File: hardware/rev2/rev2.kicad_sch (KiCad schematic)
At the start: 31 parts, among them J2 SMA, J3 SMA, J4 Antenna RF and GNSS Data, J5 Antenna GND, J7 USB_C_Receptacle_USB2.0_16P, U4 EClamp2522P

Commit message: continued routing and layouting
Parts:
- removed R24, R25: 0R, Resistor_SMD:R_0603_1608Metric_Pad0.98x0.95mm_HandSolder, symbol Device:R
- renumbered J7 to J1, R10 to R1, R11 to R2, R22 to R3, R23 to R4, U4 to U1
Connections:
- net USB_D+: now also U1.5 (DM_Out)
- net USB_D-: now also U1.4 (DP_Out)
- net D-: now reaches J1.A7 (D-), J1.B7 (D-), R3.1
- net D-*: now reaches R3.2, U1.3 (DP_In)
- net D+*: now reaches R4.2, U1.2 (DM_In)
- net D+: now reaches J1.A6 (D+), J1.B6 (D+), R4.1

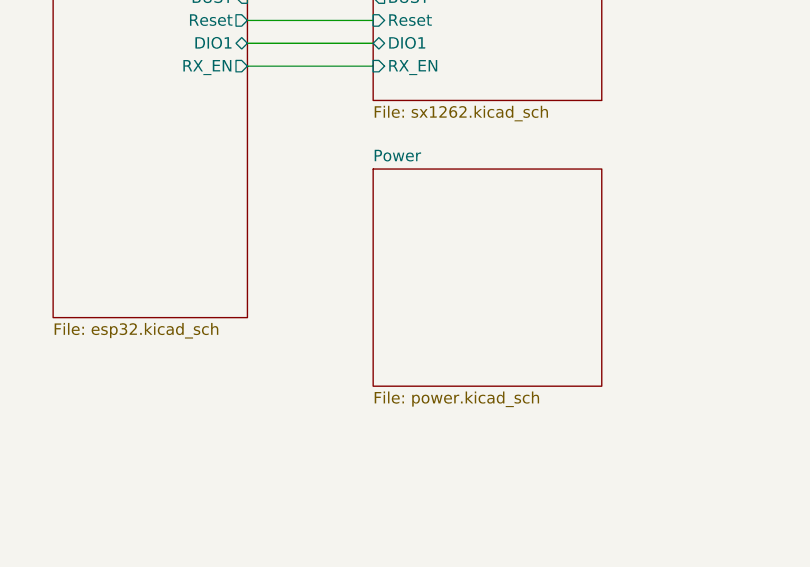
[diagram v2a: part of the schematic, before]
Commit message: Small modifications to power schematic
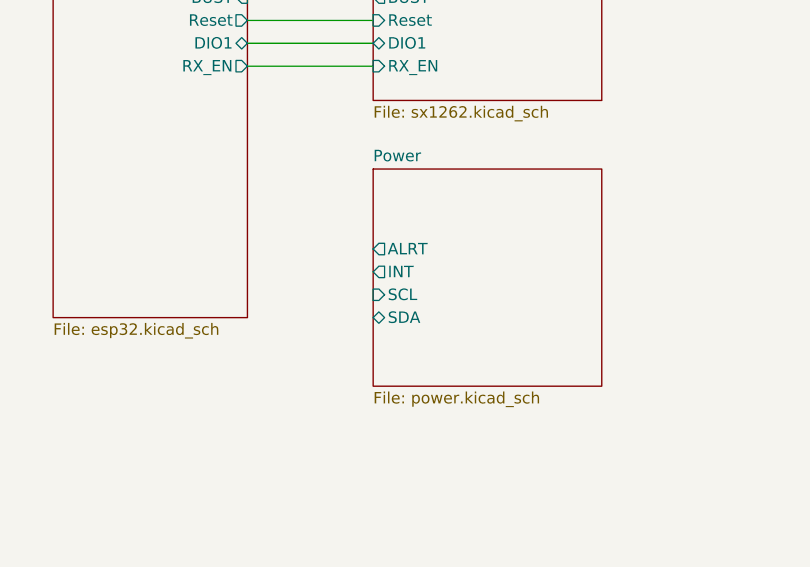
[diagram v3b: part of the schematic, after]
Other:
- sheet Power ports: added ALRT, INT, SCL, SDA; removed none
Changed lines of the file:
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@@
+			)
+		)
+		(pin "ALRT" output
+			(at 173.99 116.84 180)
+			(effects
+				(font
+					(size 1.27 1.27)
+				)
+				(justify left)
+			)
+		)
+		(pin "INT" output
+			(at 173.99 119.38 180)
+			(effects
+				(font
+					(size 1.27 1.27)
+				)
+				(justify left)
+			)
+		)
+		(pin "SCL" input
+			(at 173.99 121.92 180)
+			(effects
+				(font
+					(size 1.27 1.27)
+				)
+				(justify left)
+			)
+		)
+		(pin "SDA" bidirectional
+			(at 173.99 124.46 180)
+			(effects
+				(font
+					(size 1.27 1.27)
+				)
+				(justify left)
 			)
 		)

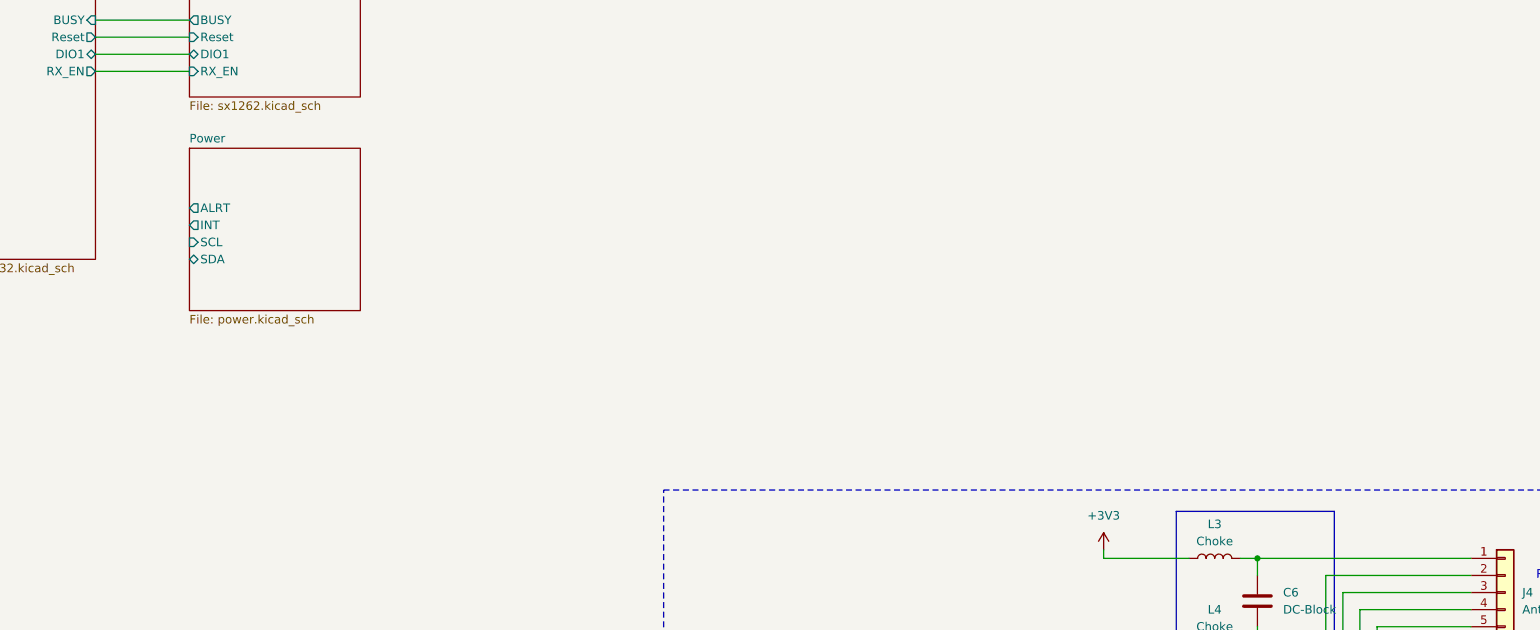
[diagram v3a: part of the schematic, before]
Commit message: continued layout, finished most of the RF stuff
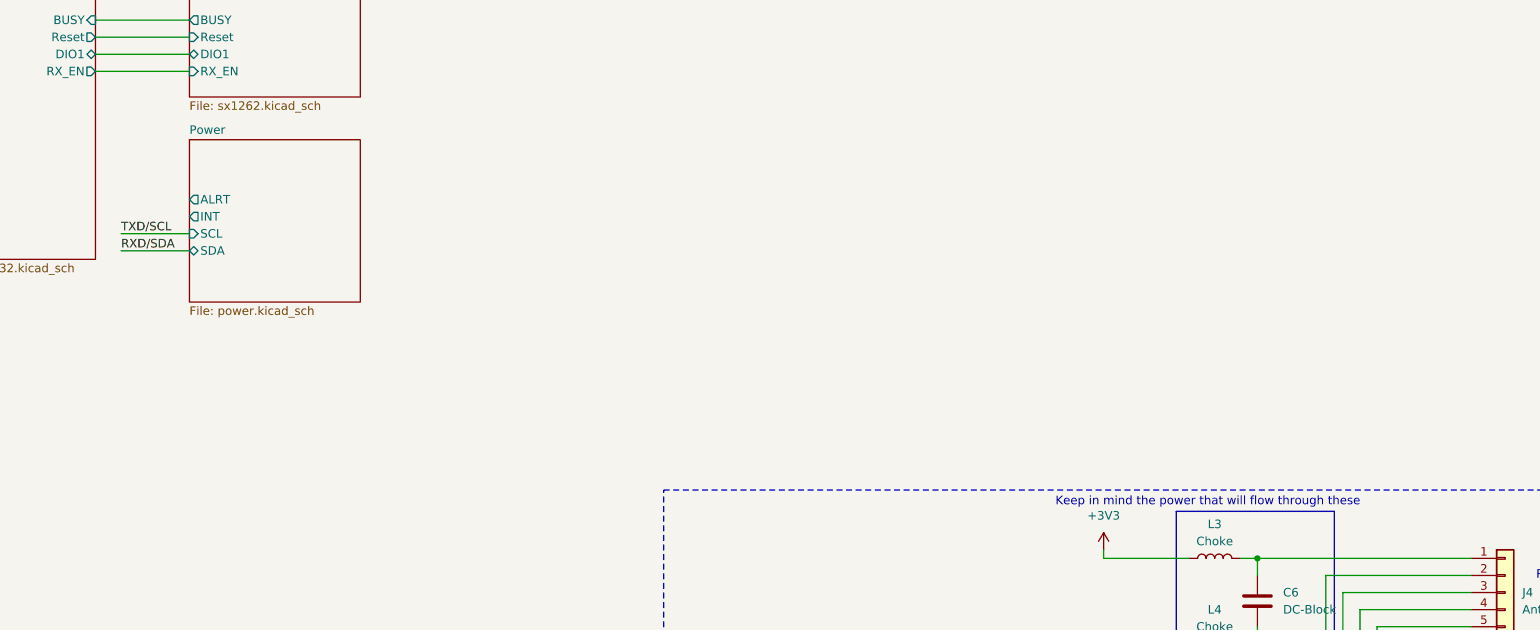
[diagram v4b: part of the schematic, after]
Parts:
- J4, J5: footprint (none) -> _footprints:Antenna_Conn
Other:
- note added: "Keep in mind the power that will flow through these"
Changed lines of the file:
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@@
 		)
 	)
+	(text "Keep in mind the power that will flow through these"
+		(exclude_from_sim no)
+		(at 325.374 160.528 0)
+		(effects
+			(font
+				(size 1.27 1.27)
+			)
+		)
+	)
 	(text "Antenna matching"
 		(exclude_from_sim no)
@@
 	(wire
 		(pts
+			(xy 163.83 123.19) (xy 173.99 123.19)
+		)
+		(stroke
+			(width 0)
+			(type default)
+		)
+	)
+	(wire
+		(pts
 			(xy 309.88 207.01) (xy 322.58 207.01)
 		)
@@
 	(wire
 		(pts
+			(xy 163.83 120.65) (xy 173.99 120.65)
+		)
+		(stroke
+			(width 0)
+			(type default)
+		)
+	)
+	(wire
+		(pts
 			(xy 364.49 195.58) (xy 364.49 198.12)
 		)
@@
 		)
 	)
+	(label "RXD{slash}SDA"
+		(at 163.83 123.19 0)
+		(effects
+			(font
+				(size 1.27 1.27)
+			)
+			(justify left bottom)
+		)
+	)
 	(label "TXD{slash}SCL"
 		(at 173.99 63.5 180)
@@
 		)
 	)
+	(label "TXD{slash}SCL"
+		(at 163.83 120.65 0)
+		(effects
+			(font
+				(size 1.27 1.27)
+			)
+			(justify left bottom)
+		)
+	)
 	(netclass_flag ""
 		(length 1.27)
@@
 			)
 		)
-		(property "Footprint" ""
+		(property "Footprint" "_footprints:Antenna_Conn"
 			(at 369.57 190.5 0)
 			(hide yes)
@@
 			)
 		)
-		(property "Footprint" ""
+		(property "Footprint" "_footprints:Antenna_Conn"
 			(at 369.57 173.99 0)
 			(hide yes)
@@
 	)
 	(sheet
-		(at 173.99 107.95)
+		(at 173.99 106.68)
 		(size 25.4 24.13)
 		(exclude_from_sim no)
@@
 		)
 		(property "Sheetname" "Power"
-			(at 173.99 107.2384 0)
+			(at 173.99 105.9684 0)
 			(show_name no)
 			(do_not_autoplace no)
@@
 		)
 		(property "Sheetfile" "power.kicad_sch"
-			(at 173.99 132.6646 0)
+			(at 173.99 131.3946 0)
 			(show_name no)
 			(do_not_autoplace no)
@@
 		)
 		(pin "ALRT" output
-			(at 173.99 116.84 180)
+			(at 173.99 115.57 180)
 			(effects
 				(font
@@
 		)
 		(pin "INT" output
-			(at 173.99 119.38 180)
+			(at 173.99 118.11 180)
 			(effects
 				(font
@@
 		)
 		(pin "SCL" input
-			(at 173.99 121.92 180)
+			(at 173.99 120.65 180)
 			(effects
 				(font
@@
 		)
 		(pin "SDA" bidirectional
-			(at 173.99 124.46 180)
+			(at 173.99 123.19 180)
 			(effects
 				(font

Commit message: modified layout
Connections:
- net D+* renamed *D+
- net D-* renamed *D-
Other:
- note added: "Interrupt pins"
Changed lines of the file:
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@@
 		)
 	)
+	(text "Interrupt pins"
+		(exclude_from_sim no)
+		(at 189.23 116.84 0)
+		(effects
+			(font
+				(size 1.27 1.27)
+			)
+		)
+	)
 	(text "Antenna matching"
 		(exclude_from_sim no)
@@
 		)
 	)
-	(label "D-*"
+	(label "*D-"
 		(at 62.23 72.39 0)
 		(effects
@@
 		)
 	)
-	(label "D+*"
+	(label "*D+"
 		(at 62.23 74.93 0)
 		(effects
@@
 	(sheet
 		(at 138.43 54.61)
-		(size 21.59 69.85)
+		(size 21.59 76.2)
 		(exclude_from_sim no)
 		(in_bom yes)
@@
 		)
 		(property "Sheetfile" "esp32.kicad_sch"
-			(at 138.43 125.0446 0)
+			(at 138.43 131.3946 0)
 			(show_name no)
 			(do_not_autoplace no)

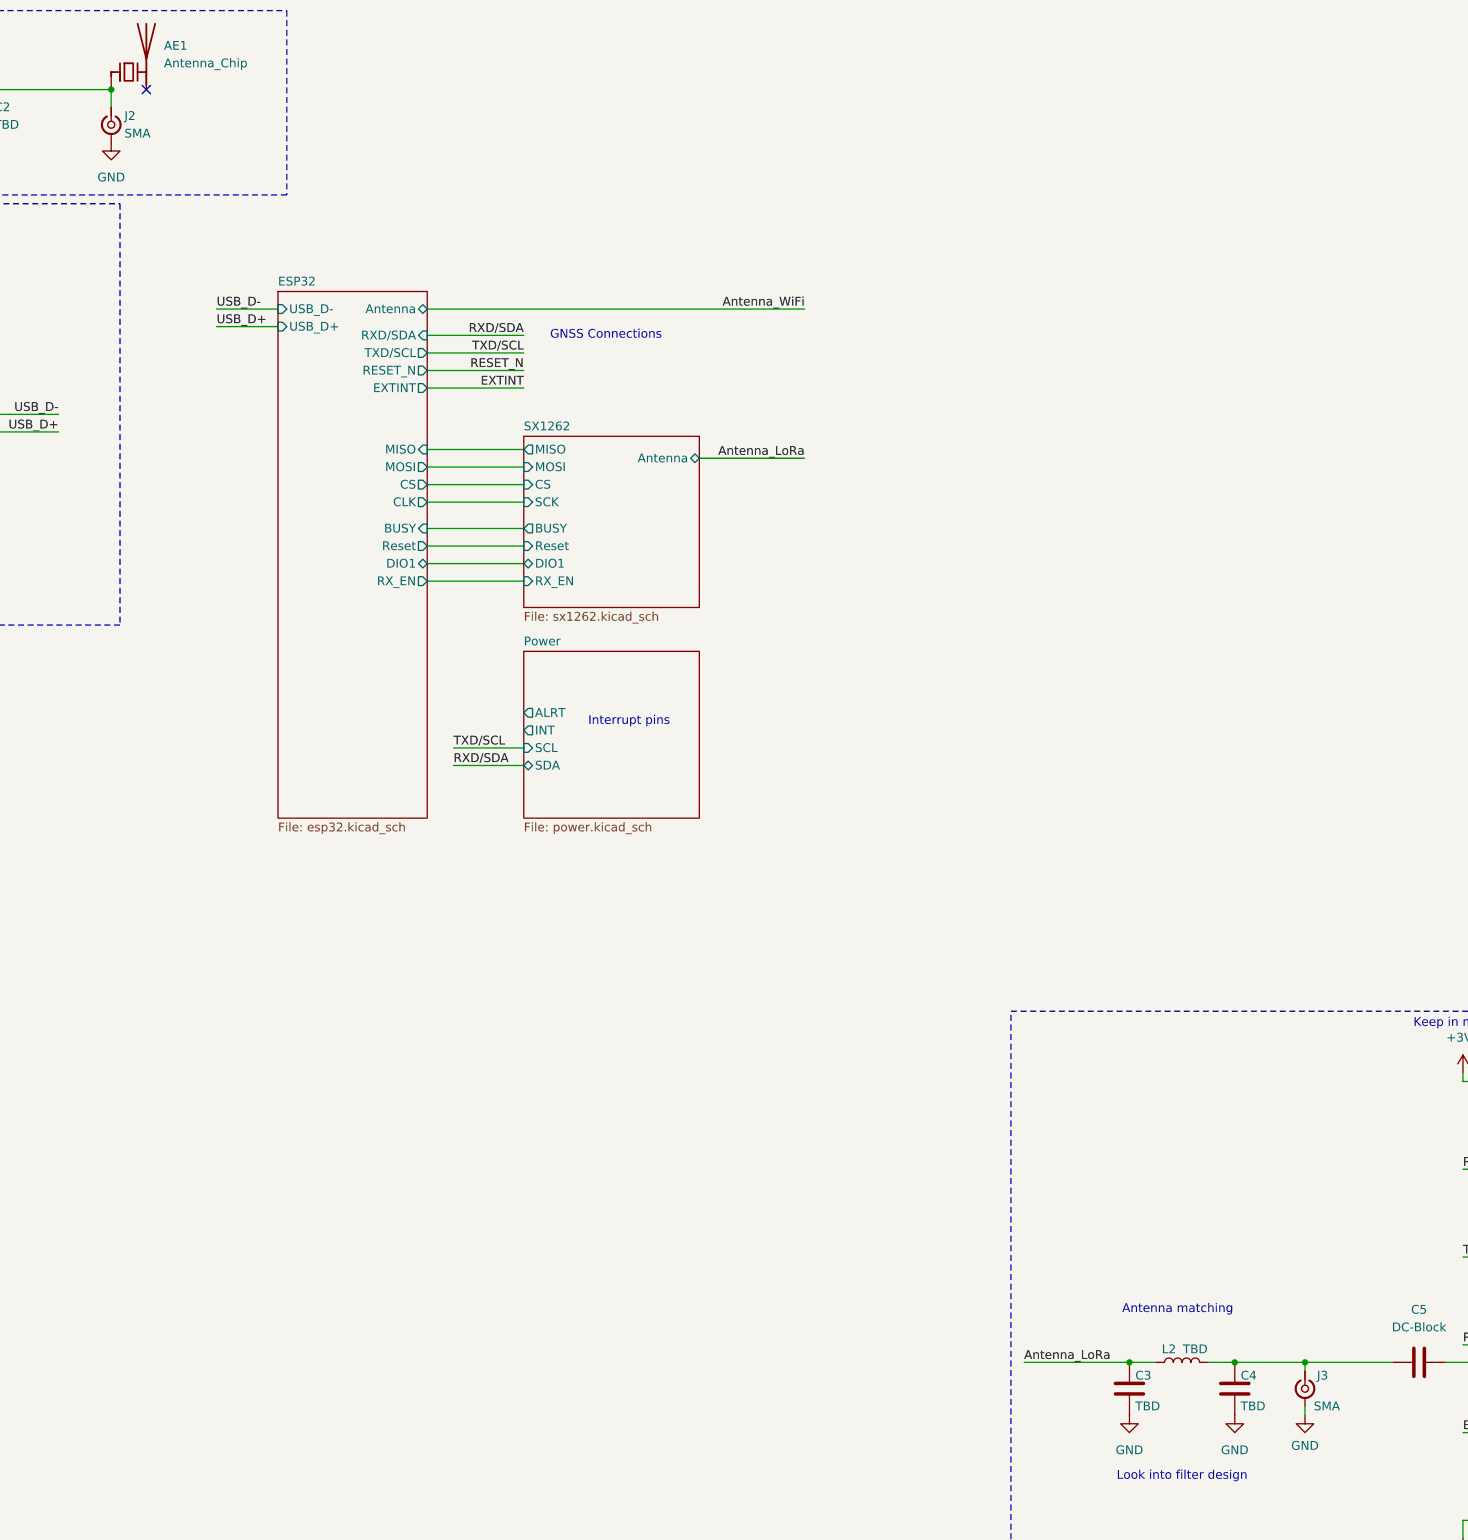
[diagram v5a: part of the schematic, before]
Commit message: finished routing most of the RF and power for SX1262 and ESP32, also decided final ish positions for both.
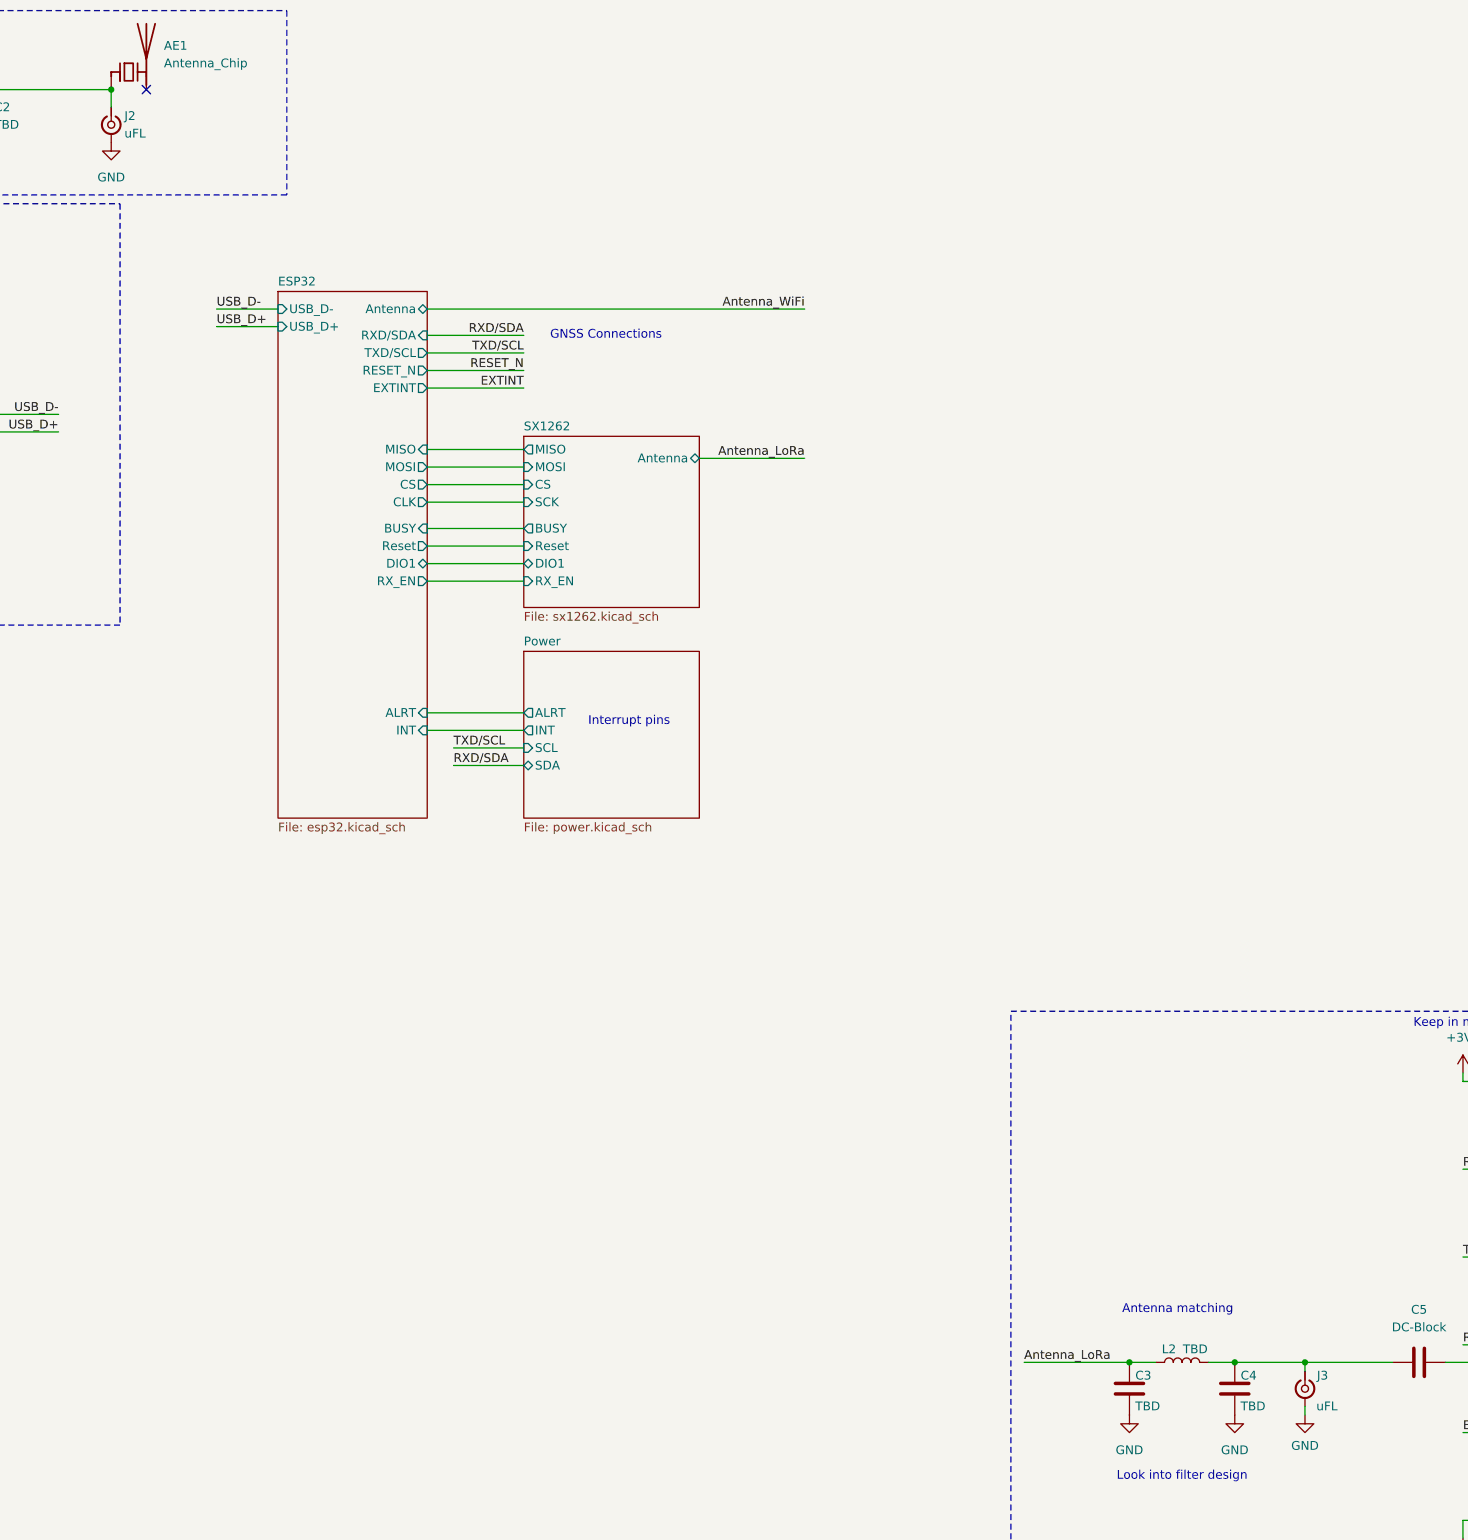
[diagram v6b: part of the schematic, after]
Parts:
- J2, J3: value SMA -> uFL
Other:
- sheet ESP32 ports: added ALRT, INT; removed none
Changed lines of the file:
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@@
 	(wire
 		(pts
+			(xy 160.02 118.11) (xy 173.99 118.11)
+		)
+		(stroke
+			(width 0)
+			(type default)
+		)
+	)
+	(wire
+		(pts
 			(xy 364.49 185.42) (xy 364.49 187.96)
 		)
@@
 	(wire
 		(pts
+			(xy 160.02 115.57) (xy 173.99 115.57)
+		)
+		(stroke
+			(width 0)
+			(type default)
+		)
+	)
+	(wire
+		(pts
 			(xy 78.74 25.4) (xy 82.55 25.4)
 		)
@@
 			)
 		)
-		(property "Value" "SMA"
+		(property "Value" "uFL"
 			(at 116.205 31.75 90)
 			(show_name no)
@@
 			)
 		)
-		(property "Value" "SMA"
+		(property "Value" "uFL"
 			(at 290.195 215.9 90)
 			(show_name no)
@@
 			(effects
 				(font
+					(size 1.27 1.27)
+				)
+				(justify right)
+			)
+		)
+		(pin "ALRT" input
+			(at 160.02 115.57 0)
+			(effects
+				(font
+					(size 1.27 1.27)
+				)
+				(justify right)
+			)
+		)
+		(pin "INT" input
+			(at 160.02 118.11 0)
+			(effects
+				(font
